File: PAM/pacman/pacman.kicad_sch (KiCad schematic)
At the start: 17 parts, among them J6 TE Mate-N-Lok, J7 TE Mate-N-Lok, J8 TE Mate-N-Lok, J9 JST PH, K1 G2RL, K2 G5V-1, Q2 MMBT2222A

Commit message: starting layout
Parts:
- removed NT1: Net-Tie_2, NetTie:NetTie-2_SMD_Pad2.0mm, symbol Device:Net-Tie_2
- added D1: LED, LED_SMD:LED_0603_1608Metric_Pad1.05x0.95mm_HandSolder, symbol Device:LED
- added J1: Conn_01x08, AERO_Footprints:TE_1-776276-1_8pin_Vertical, symbol Connector_Generic:Conn_01x08
- added J2: Conn_01x04, Connector_JST:JST_XH_B4B-XH-A_1x04_P2.50mm_Vertical, symbol Connector_Generic:Conn_01x04
- added R1: 39k, Resistor_THT:R_Axial_DIN0414_L11.9mm_D4.5mm_P25.40mm_Horizontal, symbol Device:R
- F1, F2: footprint AERO-footprints:Bell_0ADKP1000-RE -> AERO_Footprints:Bell_0ADKP1000-RE
- J6, J7, J8: footprint AERO-footprints:TE_MATE-N-LOK_1-770866-x_1x02_P4.14mm_Vertical -> AERO_Footprints:TE_MATE-N-LOK_1-770866-x_1x02_P4.14mm_Vertical
- K1: footprint AERO-footprints:G2RL -> AERO_Footprints:G2RL
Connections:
- net SHDN_IN is gone; now on net AIR_B-: D3.1 (K), K1.2, K2.10
- net AIR_B-: now also J1.3 (Pin_3)
- net GND: now also J1.8 (Pin_8), J2.4 (Pin_4)
- net INT+: now also R1.1
- net INT-: now also D1.1 (K)
- net MAIN_CONT: now also J1.6 (Pin_6)
- net PRECHARGE: now also J1.2 (Pin_2)
- new net: D1.2 (A), R1.2
- new net +12V: J1.1 (Pin_1), J2.1 (Pin_1)
- new net BMS_CAN+: J1.4 (Pin_4), J2.2 (Pin_2)
- new net BMS_CAN-: J1.5 (Pin_5), J2.3 (Pin_3)
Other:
- note added: "39k, 3W resistor"
- note added: "EMUS CAN Group Module"
- note added: "For EMUS CAN Group Module"
- note added: "HV Indicator LED"
- note added: "Pack Board - Pre/Discharge resistor circuitry - HV Indicator LED when high voltage is going out - Pass through to BMS can module"
- moved on the sheet: D3, D4, D5, F1, F2, J6, J7, J8, J9, K1, K2, Q2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

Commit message: working on layout
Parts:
- removed J6, J7, J8: TE Mate-N-Lok, AERO_Footprints:TE_MATE-N-LOK_1-770866-x_1x02_P4.14mm_Vertical, symbol Connector_Generic:Conn_01x02
- added J3, J4, J5: Conn_01x01, symbol Connector_Generic:Conn_01x01
- added J?: Conn_01x04, Connector_JST:JST_XH_B4B-XH-A_1x04_P2.50mm_Vertical, symbol Connector_Generic:Conn_01x04
- added Q?: DMN6075S, Package_TO_SOT_SMD:SOT-23, symbol Transistor_FET:DMN6075S
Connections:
- net +12V: now also J1.3 (Pin_3), J?.1 (Pin_1), J?.2 (Pin_2); no longer J1.1 (Pin_1)
- net AIR_B-: now also J1.6 (Pin_6); no longer J1.3 (Pin_3)
- net B+: now also J4.1 (Pin_1)
- net BMS_CAN+: now also J1.5 (Pin_5); no longer J1.4 (Pin_4)
- net BMS_CAN-: now also J1.8 (Pin_8); no longer J1.5 (Pin_5)
- net GND: now also J1.1 (Pin_1); no longer J1.8 (Pin_8)
- net INT+: now also J3.1 (Pin_1)
- net INT-: now also J5.1 (Pin_1)
- net MAIN_CONT: now also J1.7 (Pin_7); no longer J1.6 (Pin_6)
- net PRECHARGE: now also J1.4 (Pin_4); no longer J1.2 (Pin_2)
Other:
- note added: "BMS Fan Control -> Add in fan control from BMS, look at datasheet to see output from fan pin"
- note removed: "For EMUS CAN Group Module"

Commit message: DRC updating
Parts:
- removed J?: Conn_01x04, Connector_JST:JST_XH_B4B-XH-A_1x04_P2.50mm_Vertical, symbol Connector_Generic:Conn_01x04
- removed Q?: DMN6075S, Package_TO_SOT_SMD:SOT-23, symbol Transistor_FET:DMN6075S
- added F3: Fuse, AERO_Footprints:Fuseholder_Blade_Mini_Keystone_3568, symbol Device:Fuse
- added J6: Conn_01x02, Connector_JST:JST_XH_B2B-XH-A_1x02_P2.50mm_Vertical, symbol Connector_Generic:Conn_01x02
- added K3: G5V-1, Relay_THT:Relay_SPDT_Omron_G5V-1, symbol Relay:G5V-1
- D1: footprint LED_SMD:LED_0603_1608Metric_Pad1.05x0.95mm_HandSolder -> AERO_Footprints:LPA-C011301S-x LED 0805 LIGHT PIPE SINGLE VERT SMD
- J3, J4, J5: footprint (none) -> Connector_Hirose:Hirose_DF63M-1P-3.96DSA_1x01_P3.96mm_Vertical
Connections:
- net +12V: now also K3.2, K3.5, K3.6
- net GND: now also J6.2 (Pin_2)
- net BMS_FAN: now reaches J1.2 (Pin_2)
- net BMS_FAN: now also K3.9
- new net: F3.2, J6.1 (Pin_1)
- new net FAN_OUT: F3.1, K3.10
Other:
- note added: "BMS Fan is controlled from BMS. LOW when fan should be on"
- note added: "G5V symbol only shows pin 5. There's pin 5 and 6 on the footprint"
- note added: "Pack Fan Output"
- note removed: "BMS Fan Control -> Add in fan control from BMS, look at datasheet to see output from fan pin"

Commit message: updating side 2 mirror
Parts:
- F1, F2: footprint AERO_Footprints:Bell_0ADKP1000-RE -> AERO_Footprints:Fuseholder_Cylinder-5x20mm_Schurter_0031_8201_Horizontal_Open_3d
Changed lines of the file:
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@@
     (property "Reference" "F2" (id 0) (at 135.89 52.1462 90))
     (property "Value" "1A 300VDC" (id 1) (at 135.89 54.4576 90))
-    (property "Footprint" "AERO_Footprints:Bell_0ADKP1000-RE" (id 2) (at 135.89 55.372 90)
+    (property "Footprint" "AERO_Footprints:Fuseholder_Cylinder-5x20mm_Schurter_0031_8201_Horizontal_Open_3d" (id 2) (at 135.89 55.372 90)
       (effects (font (size 1.27 1.27)) hide)
     )
@@
     (property "Reference" "F1" (id 0) (at 135.89 44.5262 90))
     (property "Value" "1A 300VDC" (id 1) (at 135.89 46.8376 90))
-    (property "Footprint" "AERO_Footprints:Bell_0ADKP1000-RE" (id 2) (at 135.89 47.752 90)
+    (property "Footprint" "AERO_Footprints:Fuseholder_Cylinder-5x20mm_Schurter_0031_8201_Horizontal_Open_3d" (id 2) (at 135.89 47.752 90)
       (effects (font (size 1.27 1.27)) hide)
     )
@@
     )
     (path "/00000000-0000-0000-0000-00005c5231f6"
-      (reference "F1") (unit 1) (value "1A 300VDC") (footprint "AERO_Footprints:Bell_0ADKP1000-RE")
+      (reference "F1") (unit 1) (value "1A 300VDC") (footprint "AERO_Footprints:Fuseholder_Cylinder-5x20mm_Schurter_0031_8201_Horizontal_Open_3d")
     )
     (path "/00000000-0000-0000-0000-00005c5231b3"
-      (reference "F2") (unit 1) (value "1A 300VDC") (footprint "AERO_Footprints:Bell_0ADKP1000-RE")
+      (reference "F2") (unit 1) (value "1A 300VDC") (footprint "AERO_Footprints:Fuseholder_Cylinder-5x20mm_Schurter_0031_8201_Horizontal_Open_3d")
     )
     (path "/26f2172d-2d13-43ee-bfa1-5c4b7486f83c"

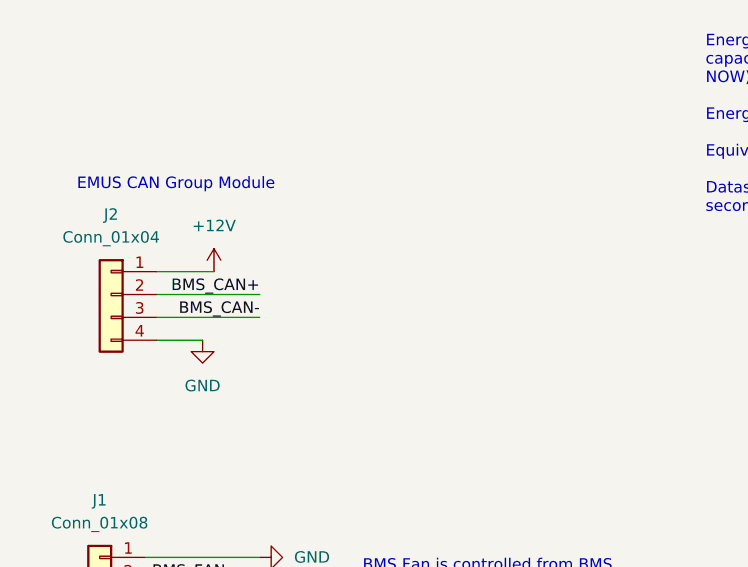
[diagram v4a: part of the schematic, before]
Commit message: Adding CAN termination resistors
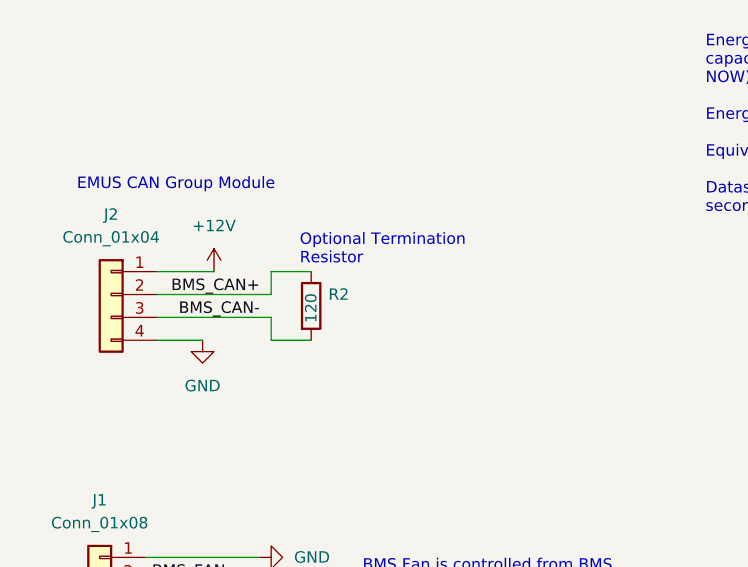
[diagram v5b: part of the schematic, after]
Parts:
- added R2: 120, Resistor_SMD:R_0603_1608Metric_Pad0.98x0.95mm_HandSolder, symbol Device:R
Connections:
- net BMS_CAN+: now also R2.1
- net BMS_CAN-: now also R2.2
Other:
- note added: "Optional Termination Resistor"
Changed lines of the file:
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@@
+    (stroke (width 0) (type default) (color 0 0 0 0))
+  )
+  (wire (pts (xy 48.26 134.62) (xy 48.26 132.08))
     (stroke (width 0) (type default) (color 0 0 0 0))
   )
@@
     (stroke (width 0) (type default) (color 0 0 0 0))
   )
-  (wire (pts (xy 35.56 134.62) (xy 46.99 134.62))
+  (wire (pts (xy 48.26 139.7) (xy 52.705 139.7))
     (stroke (width 0) (type default) (color 0 0 0 0))
   )
@@
     (stroke (width 0) (type default) (color 0 0 0 0))
   )
+  (wire (pts (xy 48.26 132.08) (xy 52.705 132.08))
+    (stroke (width 0) (type default) (color 0 0 0 0))
+  )
   (wire (pts (xy 184.15 102.87) (xy 166.37 102.87))
     (stroke (width 0) (type default) (color 0 0 0 0))
   )
-  (wire (pts (xy 35.56 137.16) (xy 46.99 137.16))
+  (wire (pts (xy 35.56 137.16) (xy 48.26 137.16))
+    (stroke (width 0) (type default) (color 0 0 0 0))
+  )
+  (wire (pts (xy 48.26 137.16) (xy 48.26 139.7))
     (stroke (width 0) (type default) (color 0 0 0 0))
   )
@@
   )
   (wire (pts (xy 34.29 176.53) (xy 52.07 176.53))
+    (stroke (width 0) (type default) (color 0 0 0 0))
+  )
+  (wire (pts (xy 35.56 134.62) (xy 48.26 134.62))
     (stroke (width 0) (type default) (color 0 0 0 0))
   )
@@
   )
   (text "Pack Fan Output" (at 151.13 162.56 0)
+    (effects (font (size 1.27 1.27)) (justify left bottom))
+  )
+  (text "Optional Termination\nResistor" (at 51.435 131.445 0)
     (effects (font (size 1.27 1.27)) (justify left bottom))
   )
@@
     )
     (property "MFR P/N" "AC07000001001JAC00" (id 4) (at 128.27 87.63 90)
+      (effects (font (size 1.27 1.27)) hide)
+    )
+    (pin "1")
+    (pin "2")
+  )
+  (symbol (lib_id "Device:R") (at 52.705 135.89 0) (unit 1)
+    (in_bom yes) (on_board yes)
+    (property "Reference" "R2" (id 0) (at 54.61 134.6199 0)
+      (effects (font (size 1.27 1.27)) (justify left))
+    )
+    (property "Value" "120" (id 1) (at 52.705 137.795 90)
+      (effects (font (size 1.27 1.27)) (justify left))
+    )
+    (property "Footprint" "Resistor_SMD:R_0603_1608Metric_Pad0.98x0.95mm_HandSolder" (id 2) (at 50.927 135.89 90)
+      (effects (font (size 1.27 1.27)) hide)
+    )
+    (property "Datasheet" "~" (id 3) (at 52.705 135.89 0)
       (effects (font (size 1.27 1.27)) hide)
     )
@@
       (reference "R1") (unit 1) (value "39k") (footprint "Resistor_THT:R_Axial_DIN0414_L11.9mm_D4.5mm_P25.40mm_Horizontal")
     )
+    (path "/06bc1d3f-a817-499c-b305-bf090751aa70"
+      (reference "R2") (unit 1) (value "120") (footprint "Resistor_SMD:R_0603_1608Metric_Pad0.98x0.95mm_HandSolder")
+    )
     (path "/00000000-0000-0000-0000-00005c5151c5"

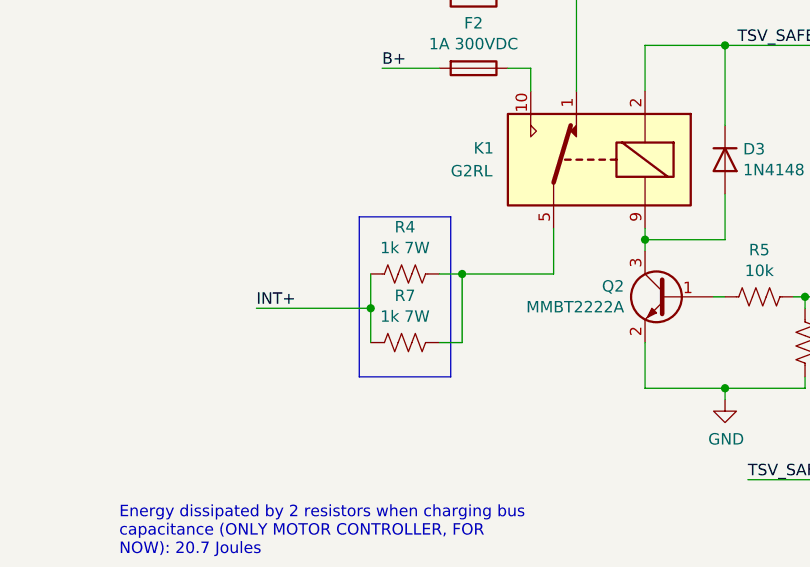
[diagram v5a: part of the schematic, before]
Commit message: Major Review and Part Update
updating footprints, component values, layouts
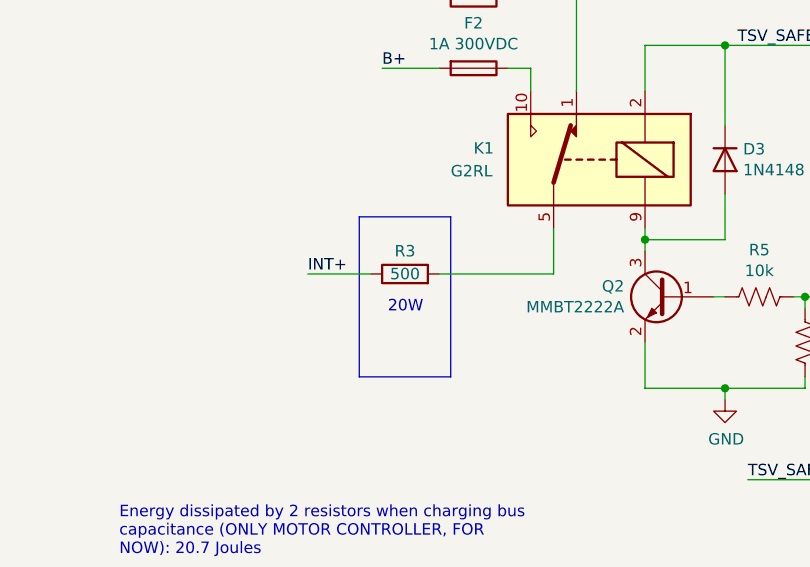
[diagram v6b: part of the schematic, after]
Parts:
- removed R4, R7: 1k 7W, Resistor_THT:R_Axial_Power_L25.0mm_W9.0mm_P30.48mm, symbol Device:R_US
- added R3: 500, Package_TO_SOT_THT:TO-220-2_Horizontal_TabDown, symbol Device:R
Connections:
- net INT+: now also R3.1
- net at K1.5, K1.6: now also R3.2
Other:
- note added: "20W"
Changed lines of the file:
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@@
   (junction (at 227.33 77.47) (diameter 0) (color 0 0 0 0)
   )
-  (junction (at 124.46 83.82) (diameter 0) (color 0 0 0 0)
-  )
   (junction (at 172.72 82.55) (diameter 0) (color 0 0 0 0)
   )
@@
   (junction (at 154.94 76.2) (diameter 0) (color 0 0 0 0)
   )
-  (junction (at 134.62 80.01) (diameter 0) (color 0 0 0 0)
-  )
   (junction (at 237.49 85.09) (diameter 0) (color 0 0 0 0)
   )
@@
     (stroke (width 0) (type default) (color 0 0 0 0))
   )
-  (wire (pts (xy 124.46 83.82) (xy 124.46 80.01))
-    (stroke (width 0) (type default) (color 0 0 0 0))
-  )
   (wire (pts (xy 132.08 57.15) (xy 125.73 57.15))
     (stroke (width 0) (type default) (color 0 0 0 0))
   )
-  (wire (pts (xy 124.46 83.82) (xy 111.76 83.82))
+  (wire (pts (xy 124.46 80.01) (xy 117.475 80.01))
     (stroke (width 0) (type default) (color 0 0 0 0))
   )
@@
     (stroke (width 0) (type default) (color 0 0 0 0))
   )
-  (wire (pts (xy 134.62 87.63) (xy 134.62 80.01))
-    (stroke (width 0) (type default) (color 0 0 0 0))
-  )
   (wire (pts (xy 31.75 35.56) (xy 39.37 35.56))
     (stroke (width 0) (type default) (color 0 0 0 0))
   )
-  (wire (pts (xy 132.08 87.63) (xy 134.62 87.63))
-    (stroke (width 0) (type default) (color 0 0 0 0))
-  )
   (wire (pts (xy 154.94 92.71) (xy 163.83 92.71))
     (stroke (width 0) (type default) (color 0 0 0 0))
@@
     (stroke (width 0) (type default) (color 0 0 0 0))
   )
-  (wire (pts (xy 134.62 80.01) (xy 144.78 80.01))
+  (wire (pts (xy 132.08 80.01) (xy 144.78 80.01))
     (stroke (width 0) (type default) (color 0 0 0 0))
   )
@@
     (stroke (width 0) (type default) (color 0 0 0 0))
   )
-  (wire (pts (xy 124.46 83.82) (xy 124.46 87.63))
-    (stroke (width 0) (type default) (color 0 0 0 0))
-  )
   (wire (pts (xy 184.15 105.41) (xy 184.15 102.87))
     (stroke (width 0) (type default) (color 0 0 0 0))
@@
   )
   (wire (pts (xy 142.24 57.15) (xy 139.7 57.15))
-    (stroke (width 0) (type default) (color 0 0 0 0))
-  )
-  (wire (pts (xy 132.08 80.01) (xy 134.62 80.01))
     (stroke (width 0) (type default) (color 0 0 0 0))
   )
@@
     (effects (font (size 1.27 1.27)) (justify left bottom))
   )
+  (text "20W\n" (at 126.365 84.455 0)
+    (effects (font (size 1.27 1.27)) (justify left bottom))
+  )
   (text "AIR Connector" (at 238.76 90.17 0)
     (effects (font (size 1.27 1.27)) (justify left bottom))
@@
     (effects (font (size 1.27 1.27)) (justify right bottom))
   )
-  (label "INT+" (at 111.76 83.82 0)
+  (label "INT+" (at 117.475 80.01 0)
     (effects (font (size 1.27 1.27)) (justify left bottom))
   )
@@
     (pin "1")
   )
-  (symbol (lib_id "Device:R_US") (at 128.27 80.01 270) (unit 1)
-    (in_bom yes) (on_board yes)
-    (property "Reference" "R4" (id 0) (at 128.27 74.803 90))
-    (property "Value" "1k 7W" (id 1) (at 128.27 77.1144 90))
-    (property "Footprint" "Resistor_THT:R_Axial_Power_L25.0mm_W9.0mm_P30.48mm" (id 2) (at 128.016 81.026 90)
-      (effects (font (size 1.27 1.27)) hide)
-    )
-    (property "Datasheet" "~" (id 3) (at 128.27 80.01 0)
-      (effects (font (size 1.27 1.27)) hide)
-    )
-    (property "MFR P/N" "AC07000001001JAC00" (id 4) (at 128.27 80.01 90)
-      (effects (font (size 1.27 1.27)) hide)
-    )
-    (pin "1")
-    (pin "2")
-  )
   (symbol (lib_id "Device:Q_NPN_BEC") (at 157.48 82.55 0) (mirror y) (unit 1)
     (in_bom yes) (on_board yes)
@@
     )
     (property "Datasheet" "http://www.nxp.com/documents/data_sheet/1N4148_1N4448.pdf" (id 3) (at 207.01 113.03 0)
-      (effects (font (size 1.27 1.27)) hide)
-    )
-    (pin "1")
-    (pin "2")
-  )
-  (symbol (lib_id "Device:R_US") (at 128.27 87.63 270) (unit 1)
-    (in_bom yes) (on_board yes)
-    (property "Reference" "R7" (id 0) (at 128.27 82.423 90))
-    (property "Value" "1k 7W" (id 1) (at 128.27 84.7344 90))
-    (property "Footprint" "Resistor_THT:R_Axial_Power_L25.0mm_W9.0mm_P30.48mm" (id 2) (at 128.016 88.646 90)
-      (effects (font (size 1.27 1.27)) hide)
-    )
-    (property "Datasheet" "~" (id 3) (at 128.27 87.63 0)
-      (effects (font (size 1.27 1.27)) hide)
-    )
-    (property "MFR P/N" "AC07000001001JAC00" (id 4) (at 128.27 87.63 90)
       (effects (font (size 1.27 1.27)) hide)
     )
@@
     (pin "1")
   )
+  (symbol (lib_id "Device:R") (at 128.27 80.01 90) (unit 1)
+    (in_bom yes) (on_board yes)
+    (property "Reference" "R3" (id 0) (at 128.27 77.47 90))
+    (property "Value" "500" (id 1) (at 128.27 80.01 90))
+    (property "Footprint" "Package_TO_SOT_THT:TO-220-2_Horizontal_TabDown" (id 2) (at 128.27 81.788 90)
+      (effects (font (size 1.27 1.27)) hide)
+    )
+    (property "Datasheet" "~" (id 3) (at 128.27 80.01 0)
+      (effects (font (size 1.27 1.27)) hide)
+    )
+    (pin "1")
+    (pin "2")
+  )
   (symbol (lib_id "Device:R") (at 33.02 80.01 0) (unit 1)
     (in_bom yes) (on_board yes) (fields_autoplaced)
@@
       (reference "R2") (unit 1) (value "120") (footprint "Resistor_SMD:R_0603_1608Metric_Pad0.98x0.95mm_HandSolder")
     )
-    (path "/00000000-0000-0000-0000-00005c5151c5"
-      (reference "R4") (unit 1) (value "1k 7W") (footprint "Resistor_THT:R_Axial_Power_L25.0mm_W9.0mm_P30.48mm")
+    (path "/d38c4111-b22d-4aa6-9f1e-02baca01bfee"
+      (reference "R3") (unit 1) (value "500") (footprint "Package_TO_SOT_THT:TO-220-2_Horizontal_TabDown")
     )
     (path "/00000000-0000-0000-0000-00005c51b36b"
@@
       (reference "R6") (unit 1) (value "2k") (footprint "Resistor_SMD:R_0603_1608Metric")
     )
-    (path "/00000000-0000-0000-0000-00005ddba44f"
-      (reference "R7") (unit 1) (value "1k 7W") (footprint "Resistor_THT:R_Axial_Power_L25.0mm_W9.0mm_P30.48mm")
-    )
-  )
+  )

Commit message: Addded comments
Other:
- note added: "*NO MORE CAN OUTPUT* Using new BMS, communication over wires not CAN network"
- note added: "*Positive to precharge"
- note added: "Pack 1"
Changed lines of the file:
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@@
+    (effects (font (size 1.27 1.27)) (justify left bottom))
+  )
+  (text "*Positive to precharge\n" (at 248.92 169.545 0)
     (effects (font (size 1.27 1.27)) (justify left bottom))
   )
@@
     (effects (font (size 1.27 1.27)) (justify left bottom))
   )
+  (text "Pack 1 \n" (at 256.54 171.45 0)
+    (effects (font (size 1.27 1.27)) (justify left bottom))
+  )
+  (text "*NO MORE CAN OUTPUT*\nUsing new BMS, communication over wires not CAN network"
+    (at 62.23 136.525 0)
+    (effects (font (size 1.27 1.27)) (justify left bottom))
+  )
